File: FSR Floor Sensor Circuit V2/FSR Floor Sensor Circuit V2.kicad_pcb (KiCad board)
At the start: 2 copper layers, 10 parts, among them J1 Daughterboard Connector, J2 MCU Connector, J3 Board Select Jumper, J4 FSR Ribbon Cable, J5 FSR Disable Jumper, U1 TMUX1308APWR

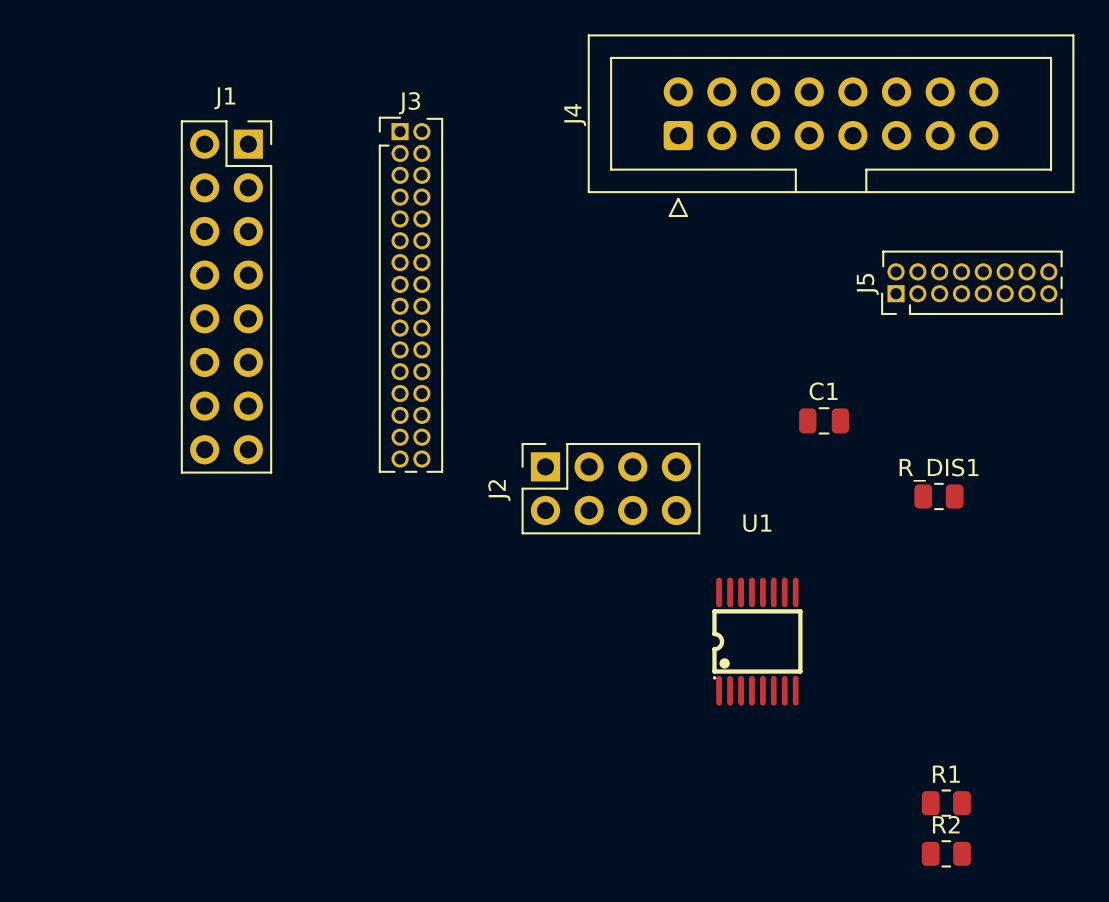
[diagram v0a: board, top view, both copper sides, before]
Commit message: daughterboard PCB layout
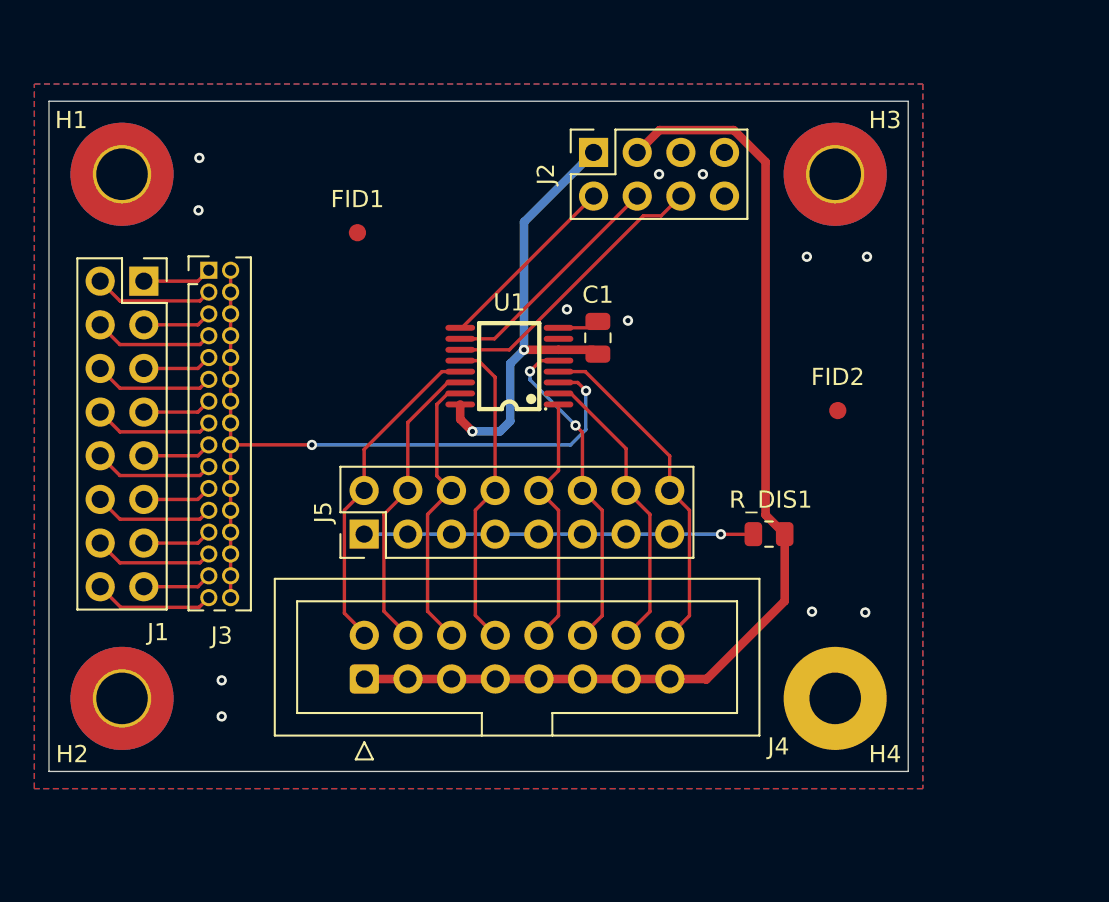
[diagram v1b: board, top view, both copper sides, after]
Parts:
- removed R1, R2: R, Resistor_SMD:R_0805_2012Metric
- added FID1: Fiducial, Fiducial:Fiducial_1mm_Mask2mm, F.Cu at (44.5, 116.8)
- added FID2: Fiducial, Fiducial:Fiducial_1mm_Mask2mm, F.Cu at (72.4, 127.2)
- added H1: MountingHole_Pad, MountingHole:MountingHole_3mm_Pad_TopBottom, F.Cu at (30.8, 113.5)
- added H2: MountingHole_Pad, MountingHole:MountingHole_3mm_Pad_TopBottom, F.Cu at (30.8, 143.9)
- added H3: MountingHole_Pad, MountingHole:MountingHole_3mm_Pad_TopBottom, F.Cu at (72.2, 113.5)
- added H4: MountingHole_Pad, MountingHole:MountingHole_3mm_Pad, F.Cu at (72.2, 143.9)
- J5: footprint Connector_PinHeader_1.27mm:PinHeader_2x08_P1.27mm_Vertical -> Connector_PinHeader_2.54mm:PinHeader_2x08_P2.54mm_Vertical
- moved J4 36.5 mm to (44.9, 142.8)
- moved J5 34.0 mm to (44.8, 134.4)
- moved U1 21.6 mm to (53.3, 124.6), turned to 90 degrees
- moved J2 18.5 mm to (58.2, 112.2)
- moved C1 14.0 mm to (58.4, 123.0), turned to 90 degrees
- moved J3 13.7 mm to (35.8, 119.0)
- moved R_DIS1 10.1 mm to (68.4, 134.4), turned to 180 degrees
- moved J1 10.0 mm to (32.0, 119.7)
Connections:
- J2 pad 2: /FSR_Mux_0 -> /FSR_Mux_2
- J2 pad 6: /FSR_Mux_2 -> /FSR_Mux_0
- J5 pad 1: /FSR Daughterboard/FSR_1 -> /FSR Daughterboard/FSR_DIS
- J5 pad 10: /FSR Daughterboard/FSR_DIS -> /FSR Daughterboard/FSR_5
- J5 pad 11: /FSR Daughterboard/FSR_6 -> /FSR Daughterboard/FSR_DIS
- J5 pad 12: /FSR Daughterboard/FSR_DIS -> /FSR Daughterboard/FSR_6
- J5 pad 13: /FSR Daughterboard/FSR_7 -> /FSR Daughterboard/FSR_DIS
- J5 pad 14: /FSR Daughterboard/FSR_DIS -> /FSR Daughterboard/FSR_7
- J5 pad 15: /FSR Daughterboard/FSR_8 -> /FSR Daughterboard/FSR_DIS
- J5 pad 16: /FSR Daughterboard/FSR_DIS -> /FSR Daughterboard/FSR_8
- J5 pad 2: /FSR Daughterboard/FSR_DIS -> /FSR Daughterboard/FSR_1
- J5 pad 3: /FSR Daughterboard/FSR_2 -> /FSR Daughterboard/FSR_DIS
- J5 pad 4: /FSR Daughterboard/FSR_DIS -> /FSR Daughterboard/FSR_2
- J5 pad 5: /FSR Daughterboard/FSR_3 -> /FSR Daughterboard/FSR_DIS
- J5 pad 6: /FSR Daughterboard/FSR_DIS -> /FSR Daughterboard/FSR_3
- J5 pad 7: /FSR Daughterboard/FSR_4 -> /FSR Daughterboard/FSR_DIS
- J5 pad 8: /FSR Daughterboard/FSR_DIS -> /FSR Daughterboard/FSR_4
- J5 pad 9: /FSR Daughterboard/FSR_5 -> /FSR Daughterboard/FSR_DIS
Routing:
- net /2V5_REF: track 0.00 -> 61.2 mm
- net /FSR Daughterboard/Selected_FSR: track 0.00 -> 44.2 mm, vias 0 -> 2
- net +5V: track 0.00 -> 26.0 mm, vias 0 -> 2
- net /FSR Daughterboard/FSR_DIS: track 0.00 -> 22.6 mm, vias 0 -> 1
- net /FSR Daughterboard/FSR_8: track 0.00 -> 19.9 mm
- net /FSR Daughterboard/FSR_6: track 0.00 -> 19.5 mm, vias 0 -> 2
- net /FSR Daughterboard/FSR_1: track 0.00 -> 19.2 mm
- net /FSR Daughterboard/FSR_4: track 0.00 -> 18.4 mm
- net /FSR Daughterboard/FSR_2: track 0.00 -> 16.8 mm
- net /FSR Daughterboard/FSR_7: track 0.00 -> 16.6 mm
- net /FSR_Mux_0: track 0.00 -> 16.5 mm
- net /FSR Daughterboard/FSR_3: track 0.00 -> 15.8 mm
- net /FSR Daughterboard/FSR_5: track 0.00 -> 14.9 mm
- net /FSR_Mux_1: track 0.00 -> 13.7 mm
- net /FSR_Mux_2: track 0.00 -> 10.9 mm
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- added copper zone on B.Cu, net GND
- added copper zone on F.Cu, net GND
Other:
- board outline added: 50 x 39 mm

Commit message: fix mounting hole and cleanup
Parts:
- H4: footprint MountingHole:MountingHole_3mm_Pad -> MountingHole:MountingHole_3mm_Pad_TopBottom
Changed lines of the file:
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@@
 		(capping no)
 		(filling no)
-		(zone_defaults)
 		(grid_origin 26.5 131.6)
 		(pcbplotparams
@@
 		)
 	)
-	(footprint "MountingHole:MountingHole_3mm_Pad"
-		(locked yes)
+	(footprint "MountingHole:MountingHole_3mm_Pad_TopBottom"
 		(layer "F.Cu")
 		(at 72.25 143.95)
@@
 		(tags "mountinghole")
 		(property "Reference" "H4"
-			(at 2.9 3.25 0)
+			(at 0 -3.95 0)
 			(layer "F.SilkS")
 			(effects
@@
 		(pad "1" thru_hole circle
 			(at 0 0)
-			(size 6 6)
+			(size 3.4 3.4)
 			(drill 3)
 			(layers "*.Cu" "*.Mask")
@@
 			(zone_connect 2)
 		)
+		(pad "1" connect circle
+			(at 0 0)
+			(size 6 6)
+			(layers "F.Cu" "F.Mask")
+			(net "GND")
+			(pinfunction "1_1")
+			(pintype "input")
+			(zone_connect 2)
+		)
+		(pad "1" connect circle
+			(at 0 0)
+			(size 6 6)
+			(layers "B.Cu" "B.Mask")
+			(net "GND")
+			(pinfunction "1_1")
+			(pintype "input")
+			(zone_connect 2)
+		)
 		(embedded_fonts no)
 	)
@@
 			)
 		)
-		(property "KiLib_Generator" "connector/pin_header_socket"
-			(at 0 0 90)
-			(layer "F.SilkS")
-			(hide yes)
-			(effects
-				(font
-					(size 1 1)
-					(thickness 0.15)
-				)
-			)
-		)
 		(property ki_fp_filters "Connector*:*_2x??_*")
 		(sheetname "/FSR Daughterboard/")
 		(sheetfile "fsr_daughterboard.kicad_sch")
+		(units
+			(unit
+				(name "A")
+				(pins "1" "3" "5" "7" "9" "11" "13" "15" "2" "4" "6" "8" "10" "12" "14"
+					"16"
+				)
+			)
+		)
 		(attr through_hole)
 		(duplicate_pad_numbers_are_jumpers no)
@@
 		(width 0.2)
 		(layer "F.Cu")
-		(net "/FSR_Mux_2")
-	)
-	(segment
-		(start 50.43 122.385)
-		(end 50.525 122.385)
-		(width 0.2)
-		(layer "F.Cu")

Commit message: minor pcb cleanup
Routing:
- net /FSR_Mux_2: track 10.8 -> 11.5 mm
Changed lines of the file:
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@@
 		(tags "mountinghole")
 		(property "Reference" "H1"
-			(at -2.95 -3.15 0)
+			(at 4.85 0.55 0)
 			(layer "F.SilkS")
 			(effects
@@
 		(tags "mountinghole")
 		(property "Reference" "H3"
-			(at 2.9 -3.15 0)
+			(at 0.15 4.5 0)
 			(layer "F.SilkS")
 			(effects
@@
 		(tags "mountinghole")
 		(property "Reference" "H2"
-			(at -2.9 3.25 0)
+			(at 5.4 0.05 0)
 			(layer "F.SilkS")
 			(effects
@@
 		(start 56.15 122.385)
 		(end 58.07 122.385)
-		(width 0.2)
+		(width 0.4)
 		(layer "F.Cu")
 		(net "GND")
@@
 	)
 	(via
-		(at 36.55 145)
+		(at 35.95 146.1)
 		(size 0.6)
 		(drill 0.3)
@@
 	)
 	(via
-		(at 36.55 142.9)
+		(at 35.95 142.2)
 		(size 0.6)
 		(drill 0.3)
@@
 	)
 	(via
-		(at 56.64 121.315)
+		(at 58.4 120.35)
 		(size 0.6)
 		(drill 0.3)
@@
 	)
 	(segment
+		(start 51.615 122.385)
+		(end 58.19 115.81)
+		(width 0.2)
+		(layer "F.Cu")
+		(net "/FSR_Mux_2")
+	)
+	(segment
 		(start 50.525 122.385)
+		(end 51.615 122.385)
+		(width 0.2)
+		(layer "F.Cu")
+		(net "/FSR_Mux_2")
+	)
+	(segment
+		(start 58.19 115.81)
 		(end 58.19 114.72)
 		(width 0.2)
@@
 	)
 	(segment
-		(start 50.43 123.665)
-		(end 53.291471 123.665)
+		(start 53.291471 123.665)
+		(end 60.056471 116.9)
 		(width 0.2)
 		(layer "F.Cu")
@@
 	)
 	(segment
-		(start 53.291471 123.665)
-		(end 61.086471 115.87)
+		(start 61.09 116.9)
+		(end 63.27 114.72)
 		(width 0.2)
 		(layer "F.Cu")
@@
 	)
 	(segment
-		(start 62.12 115.87)
-		(end 63.27 114.72)
+		(start 60.056471 116.9)
+		(end 61.09 116.9)
 		(width 0.2)
 		(layer "F.Cu")
@@
 	)
 	(segment
-		(start 61.086471 115.87)
-		(end 62.12 115.87)
+		(start 50.43 123.665)
+		(end 53.291471 123.665)
 		(width 0.2)
 		(layer "F.Cu")

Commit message: via and trace cleanup, better ground plane connectivity
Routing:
- net GND: vias 12 -> 14
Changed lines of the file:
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@@
+	)
+	(via
+		(at 55.4 116.9)
+		(size 0.6)
+		(drill 0.3)
+		(layers "F.Cu" "B.Cu")
+		(free yes)
+		(net "GND")
 	)
 	(via
@@
 		(size 0.6)
 		(drill 0.3)
+		(layers "F.Cu" "B.Cu")
+		(free yes)
+		(net "GND")
+	)
+	(via
+		(at 56.3 116)
+		(size 0.6)
+		(drill 0.3)
